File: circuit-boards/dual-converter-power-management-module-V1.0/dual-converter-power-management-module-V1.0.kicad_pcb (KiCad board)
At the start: 4 copper layers, 38 x 70 mm, 64 parts, among them J1 Conn_02x03_Odd_Even, J2 Conn_01x06_Pin, J3 Conn_02x03_Odd_Even, J4 Conn_02x03_Odd_Even, J5 Conn_02x03_Odd_Even, U1 TPS1HTC30AQPWPRQ1

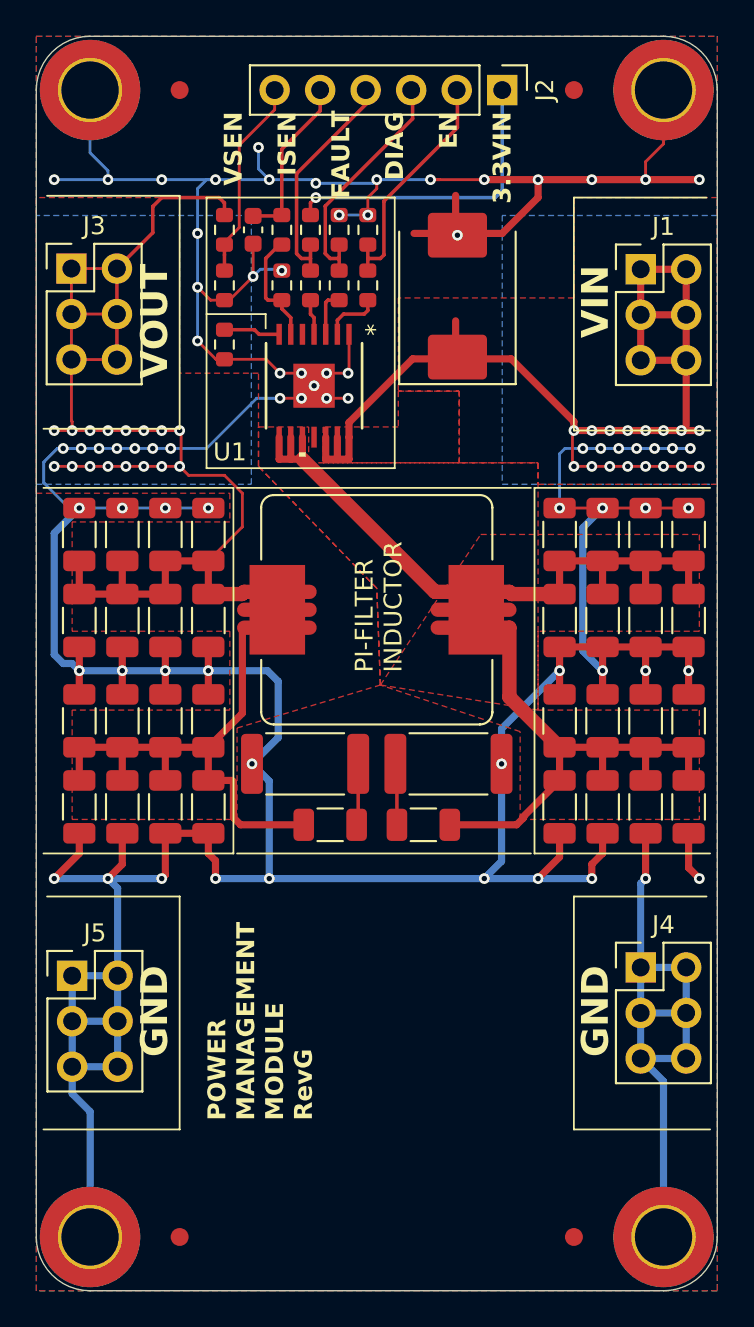
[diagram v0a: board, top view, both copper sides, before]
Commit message: powerman: align and lock connectors and mountpoints, increase clearance and spacing on high voltage traces
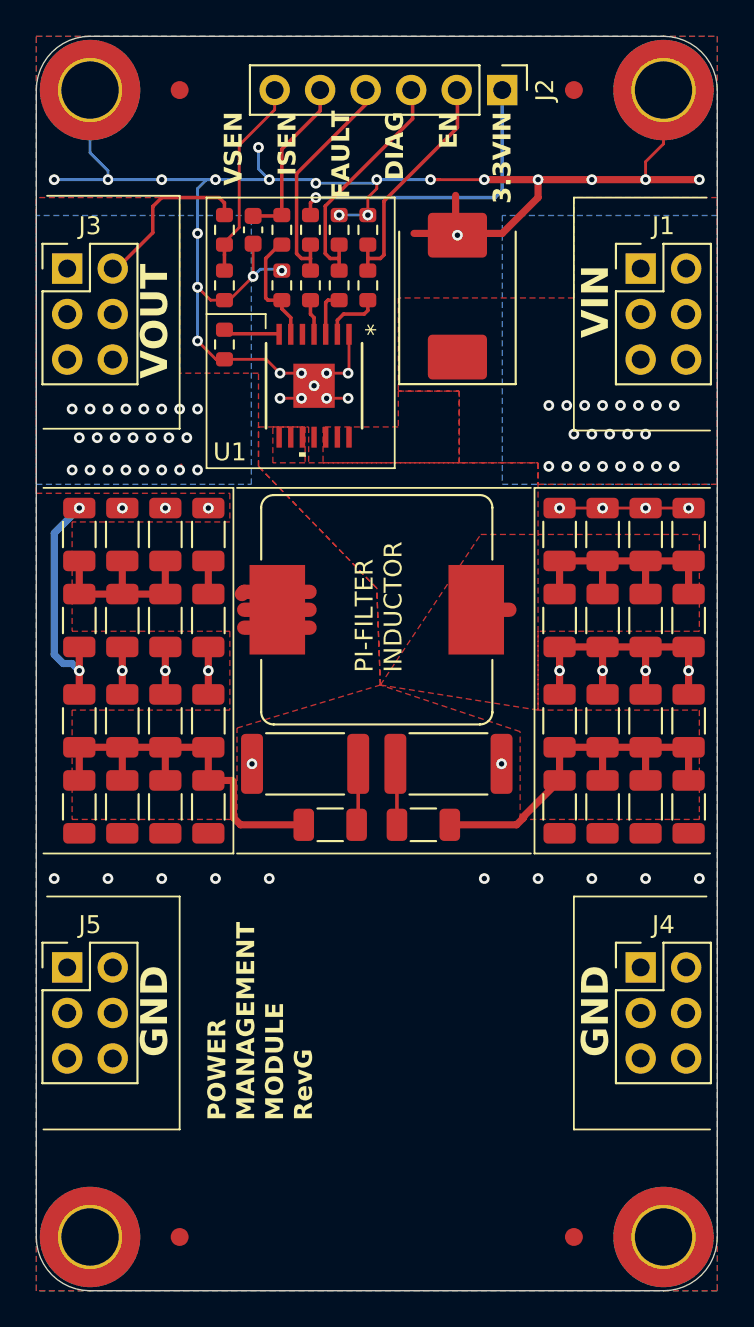
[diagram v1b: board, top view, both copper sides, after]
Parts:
- moved J5 0.54 mm to (38.7, 89.0)
- moved J3 0.23 mm to (38.7, 50.0)
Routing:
- net GND: track 346.3 -> 137.7 mm, vias 73 -> 71
- net +48VIN: track 59.1 -> 0.00 mm
- net +48V: track 113.4 -> 55.3 mm
- net /FILTER_IN: track 73.9 -> 38.3 mm
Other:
- board text added: "increase space between 48V and gnd flood fills and traces by.... a lot"
